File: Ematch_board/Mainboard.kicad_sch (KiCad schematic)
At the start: 78 parts, among them J10 Conn_01x02_Male, J7 Conn_01x05_Male, J8 USB_C_Receptacle_USB2.0, J9 Conn_01x02_Male, Q1 MMDT2222A, Q2 MMDT2222A, U2 LTC4411, U3 RT9025-25GSP, U4 LTC4411, U5 SN65HVD230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

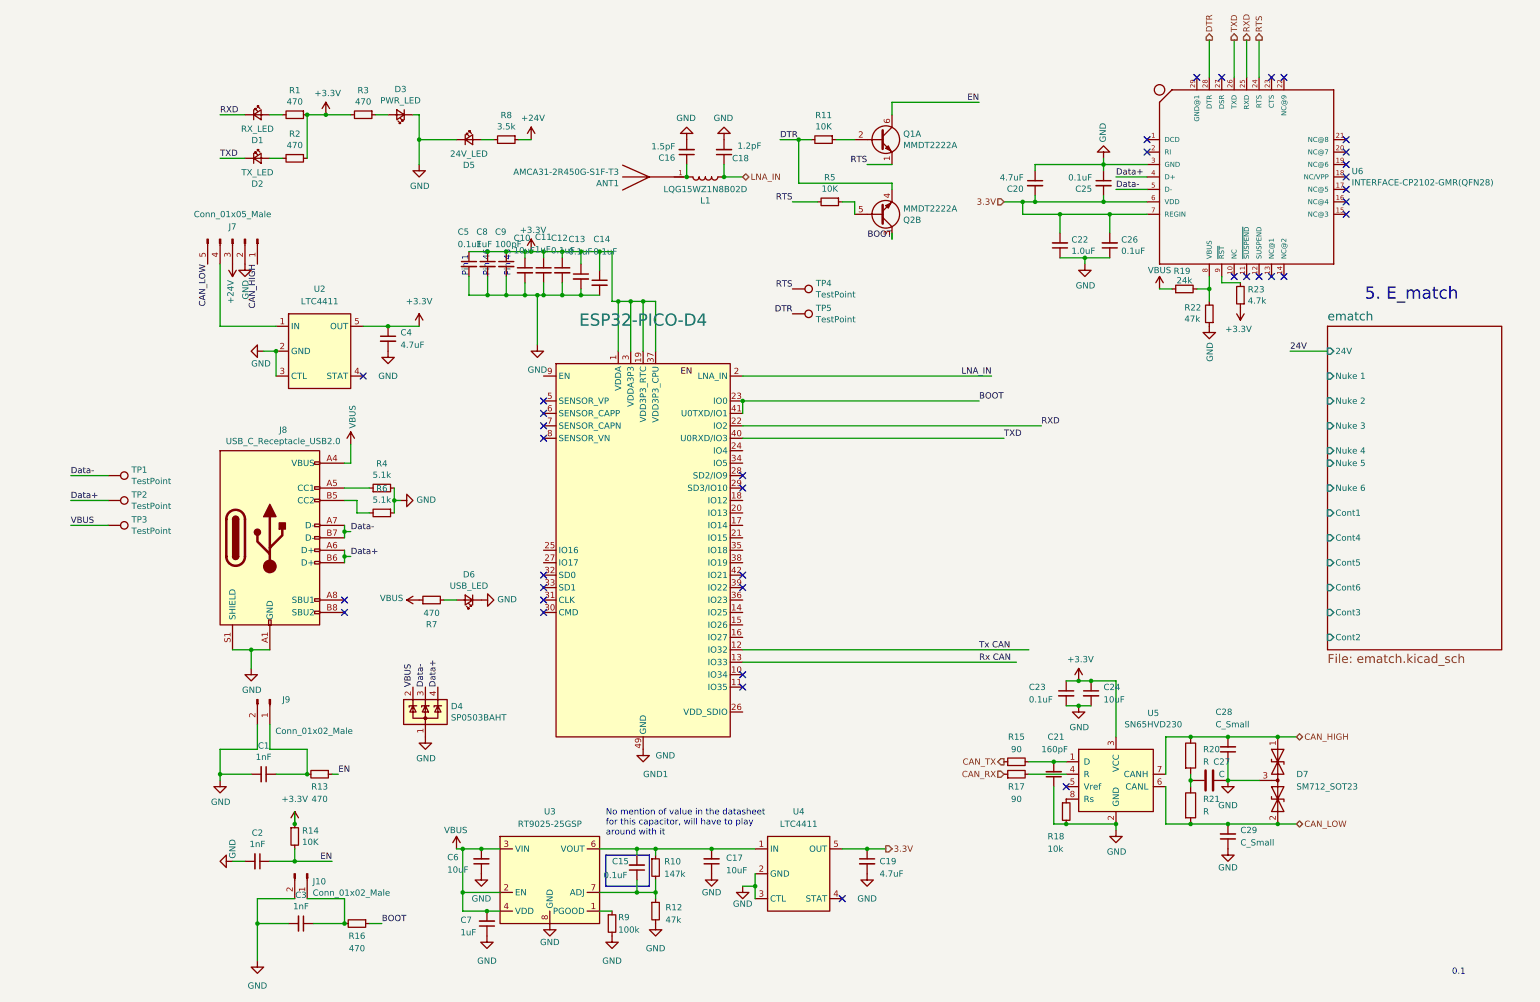
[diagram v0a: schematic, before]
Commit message: changed LDO passives, changed filestructure
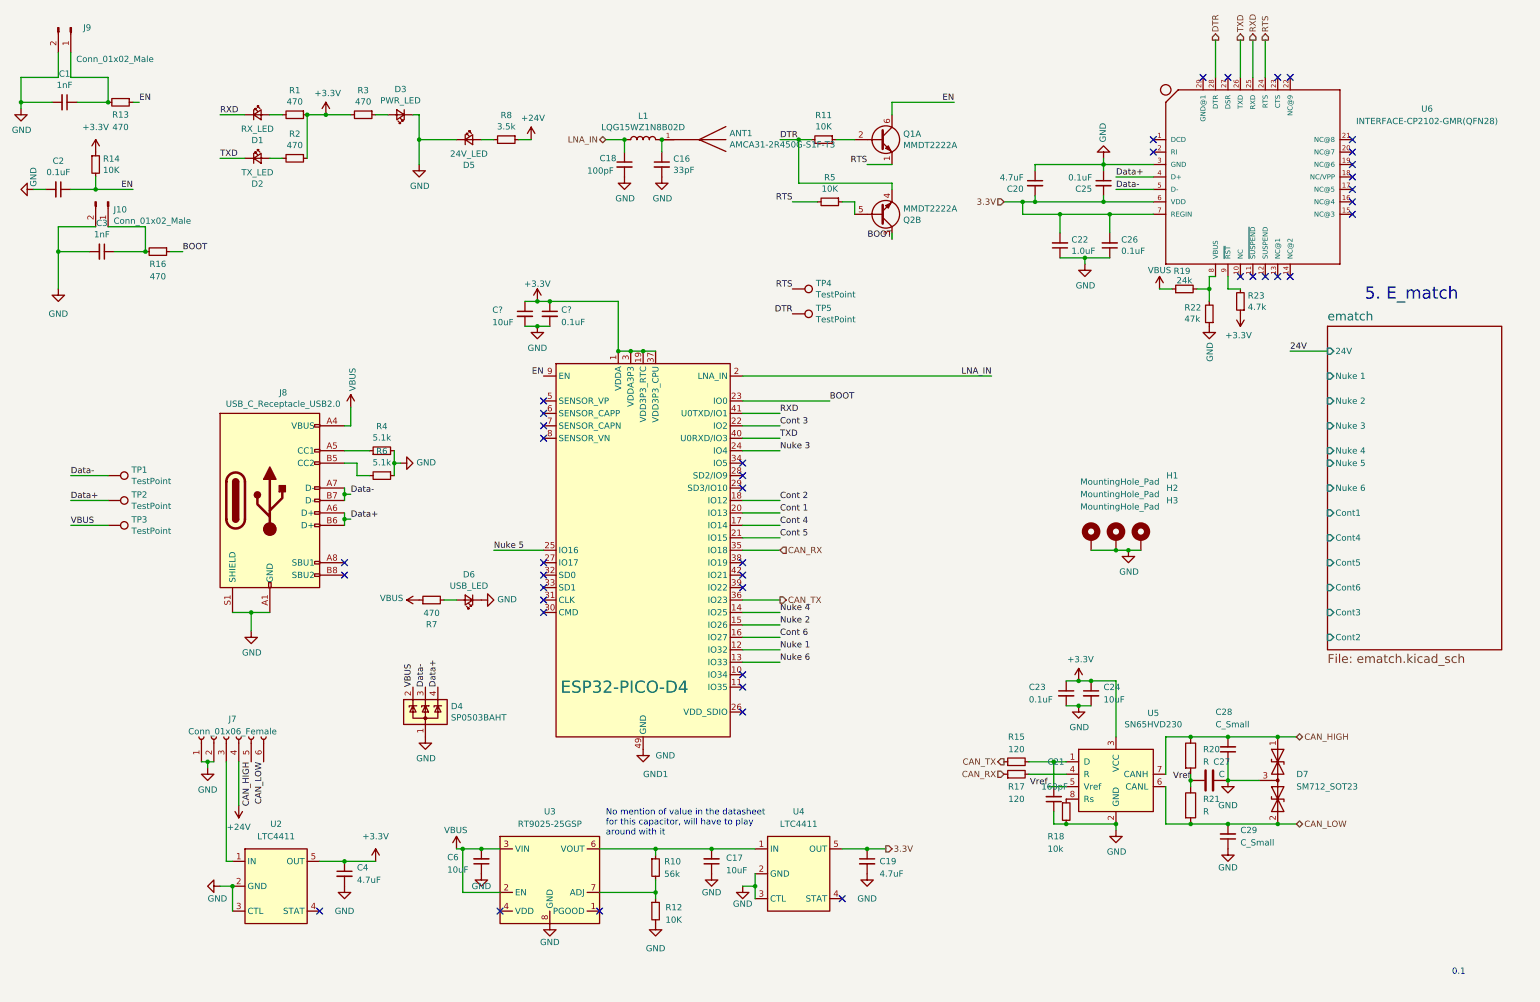
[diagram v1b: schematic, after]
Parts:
- removed C10: 10uF, Capacitor_SMD:C_0603_1608Metric, symbol Device:C_Small
- removed C11, C7, C8: 1uF, Capacitor_SMD:C_0603_1608Metric, symbol Device:C_Small
- removed C12, C13, C14, C15, C5: 0.1uF, Capacitor_SMD:C_0603_1608Metric, symbol Device:C_Small
- removed C9: 100pF, Capacitor_SMD:C_0603_1608Metric, symbol Device:C_Small
- removed J7: Conn_01x05_Male, Connector_PinHeader_2.54mm:PinHeader_1x05_P2.54mm_Vertical, symbol Connector:Conn_01x05_Male
- removed R9: 100k, Resistor_SMD:R_0603_1608Metric, symbol Device:R_Small
- added C?: 10uF, symbol Device:C_Small
- added C?: 0.1uF, symbol Device:C_Small
- added H1, H2, H3: MountingHole_Pad, MountingHole:MountingHole_3.2mm_M3_DIN965_Pad, symbol Mechanical:MountingHole_Pad
- added J7: Conn_01x06_Female, Connector_Molex:Molex_Mini-Fit_Jr_5566-06A_2x03_P4.20mm_Vertical, symbol Connector:Conn_01x06_Female
- C16: value 1.5pF -> 33pF
- C18: value 1.2pF -> 100pF
- C2: value 1nF -> 0.1uF
- C21, C23, C24, C27, C28, C29: footprint (none) -> Capacitor_SMD:C_0603_1608Metric
- R10: value 147k -> 56k
- R12: value 47k -> 10K
- R15, R17: value 90 -> 120; footprint (none) -> Resistor_SMD:R_0603_1608Metric
- R18, R20, R21: footprint (none) -> Resistor_SMD:R_0603_1608Metric
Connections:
- net +24V: now also J7.4 (Pin_4)
- net +3V3: now also C?.1, C?.1
- net BOOT: no longer GND1.41 (U0TXD/IO1)
- net CAN_HIGH: now also J7.5 (Pin_5)
- net CAN_LOW: now also J7.6 (Pin_6)
- net CAN_RX: now also GND1.35 (IO18)
- net CAN_TX: now also GND1.36 (IO23)
- net EN: now also GND1.9 (EN)
- net GND: now also C?.2, C?.2, H1.1, H2.1, H3.1, J7.1 (Pin_1), J7.2 (Pin_2)
- net RXD: now also GND1.41 (U0TXD/IO1); no longer GND1.22 (IO2)
- net VBUS: no longer U3.4 (VDD)
- net Nuke 4: now reaches GND1.14 (IO25)
- net Nuke 2: now reaches GND1.15 (IO26)
- net Cont 6: now reaches GND1.16 (IO27)
- net Cont 4: now reaches GND1.17 (IO14)
- net Cont 2: now reaches GND1.18 (IO12)
- net Cont 1: now reaches GND1.20 (IO13)
- net Cont 5: now reaches GND1.21 (IO15)
- net Nuke 3: now reaches GND1.24 (IO4)
- net Nuke 5: now reaches GND1.25 (IO16)
- net Vref: now reaches C27.1, R20.2, R21.1
- net Vref: now also U5.5 (Vref)
- net at U2.1 (IN): now also J7.3 (Pin_3)
- net Rx CAN renamed Nuke 6
- net Tx CAN renamed Nuke 1
- new net Cont 3: GND1.22 (IO2)
- no-connect marks 37 -> 42
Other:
- note removed: "Pin 1"
- note removed: "Pin 43"
- note removed: "Pin 46"
- moved on the sheet: ANT1, C1, C16, C18, C2, C21, C3, C4, J10, J8, J9, L1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
